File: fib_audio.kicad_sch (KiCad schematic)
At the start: 64 parts, among them IC1 ICS-43434, IC2 ICS-43434, IC3 ICS-43434, IC4 ICS-43434, J3 Conn_01x02, J8 SJ2-35954D-SMT-TR, J9 Conn_01x02, U701 WM8960CGEFL, X701 24MHz 306020014

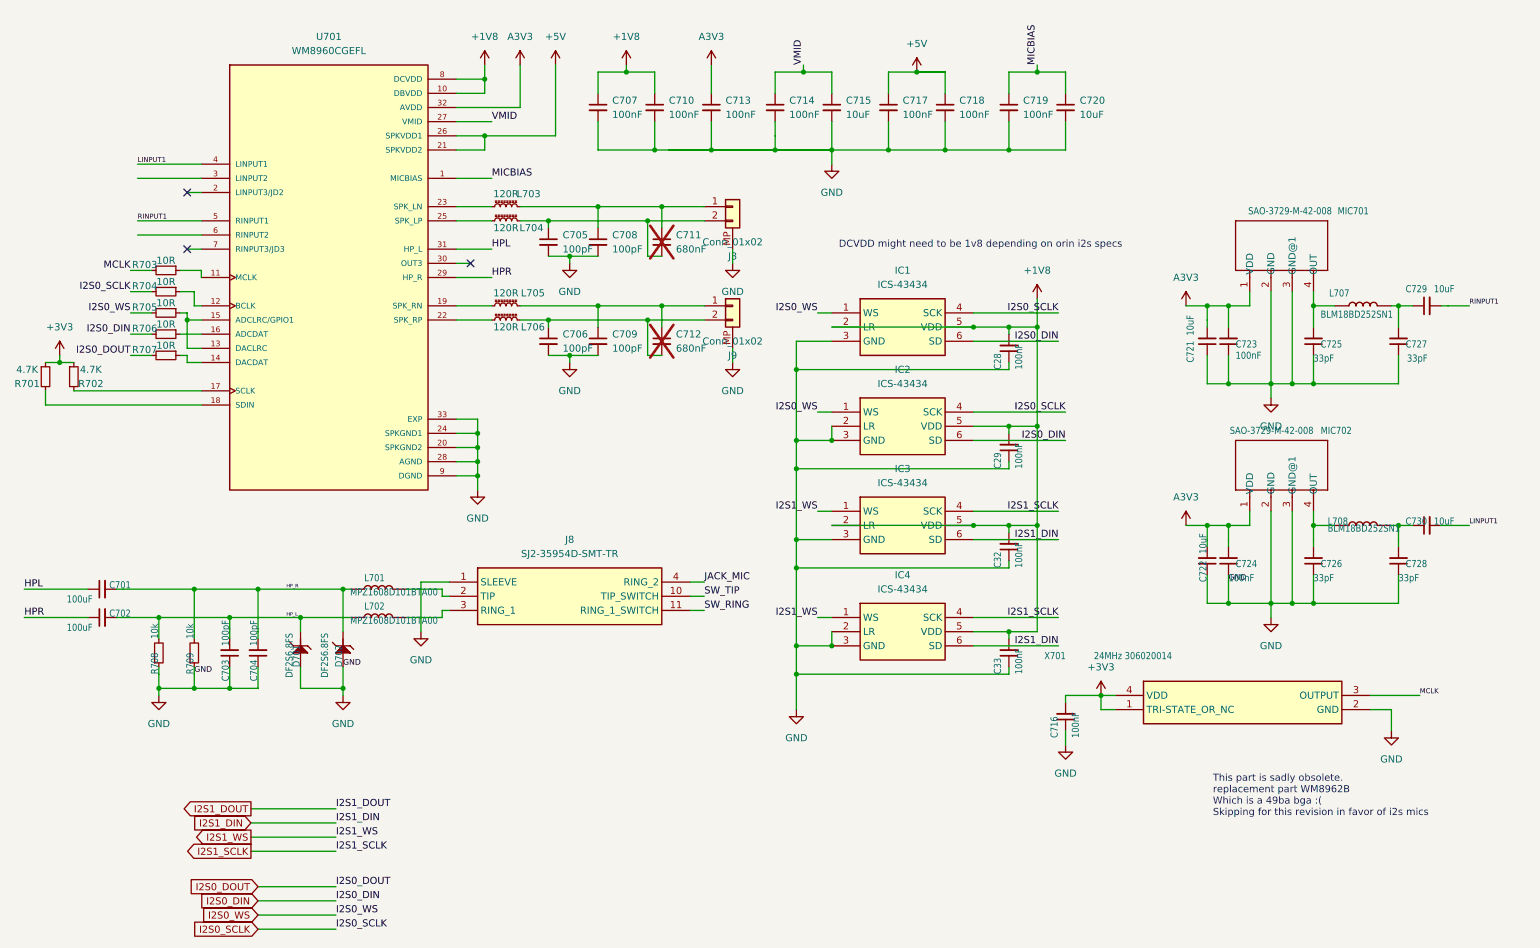
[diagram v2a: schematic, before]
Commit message: adde testpoints, fixed power supplies, ready to order
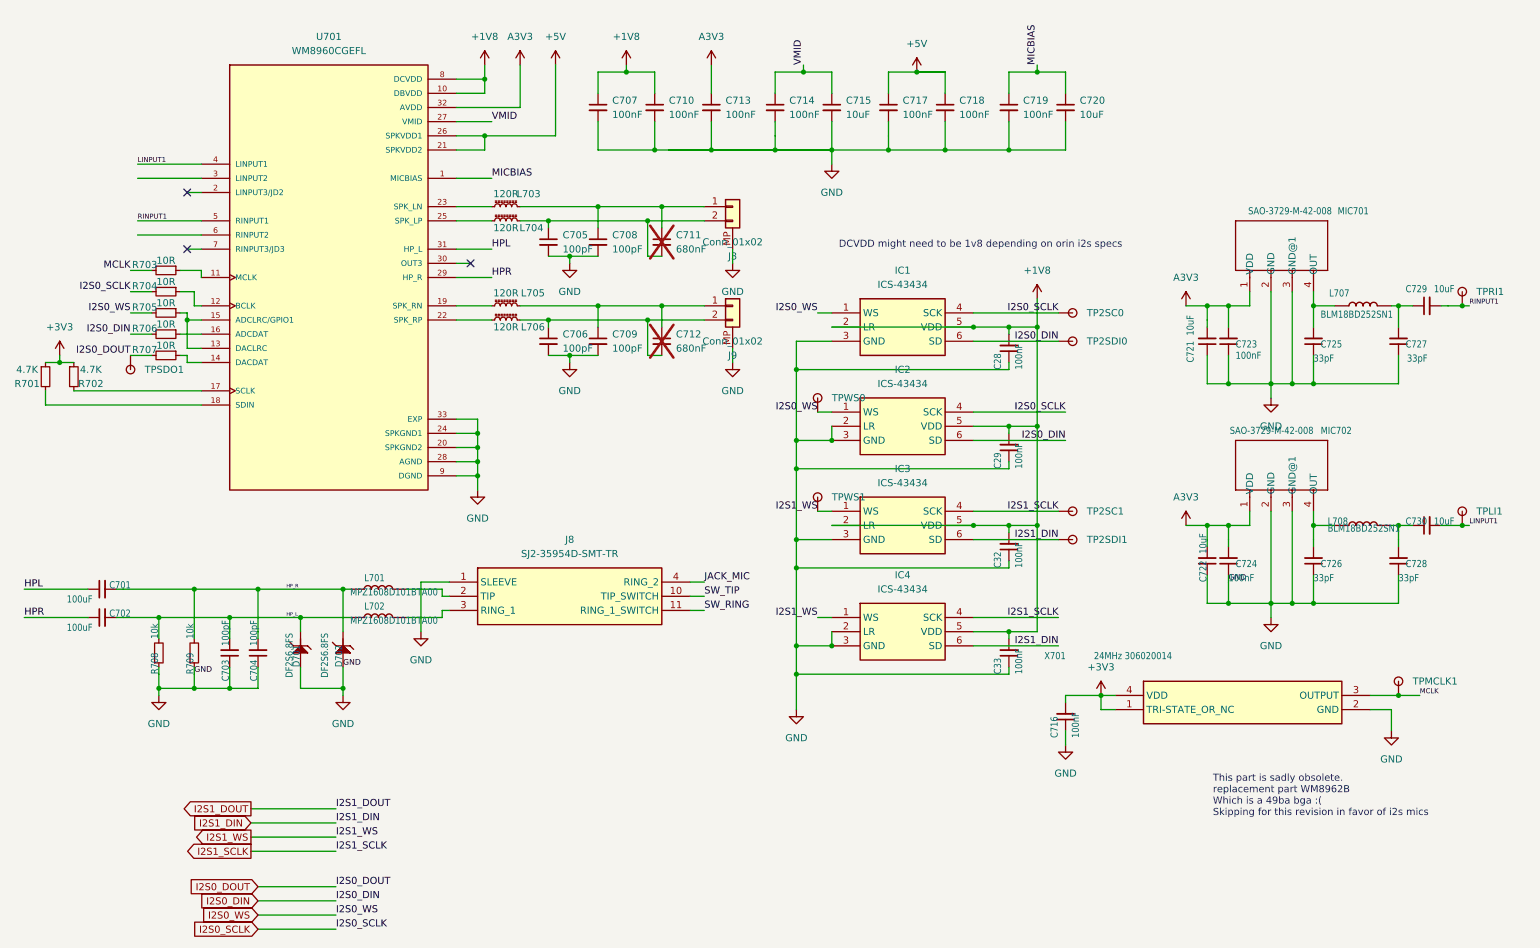
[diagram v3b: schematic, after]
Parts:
- added TP2SC0, TP2SC1, TP2SDI0, TP2SDI1, TPLI1, TPMCLK1, TPRI1, TPSDO1, TPWS0, TPWS1: TestPoint, TestPoint:TestPoint_Pad_D1.0mm, symbol Fibel2:TestPoint
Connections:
- net I2S0_DIN: now also TP2SDI0.1
- net I2S0_DOUT: now also TPSDO1.1
- net I2S0_SCLK: now also TP2SC0.1
- net I2S0_WS: now also TPWS0.1
- net I2S1_DIN: now also TP2SDI1.1
- net I2S1_SCLK: now also TP2SC1.1
- net I2S1_WS: now also TPWS1.1
- net LINPUT1: now also TPLI1.1
- net MCLK: now also TPMCLK1.1
- net RINPUT1: now also TPRI1.1
